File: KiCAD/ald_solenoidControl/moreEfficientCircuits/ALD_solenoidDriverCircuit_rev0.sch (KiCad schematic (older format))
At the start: 36 parts

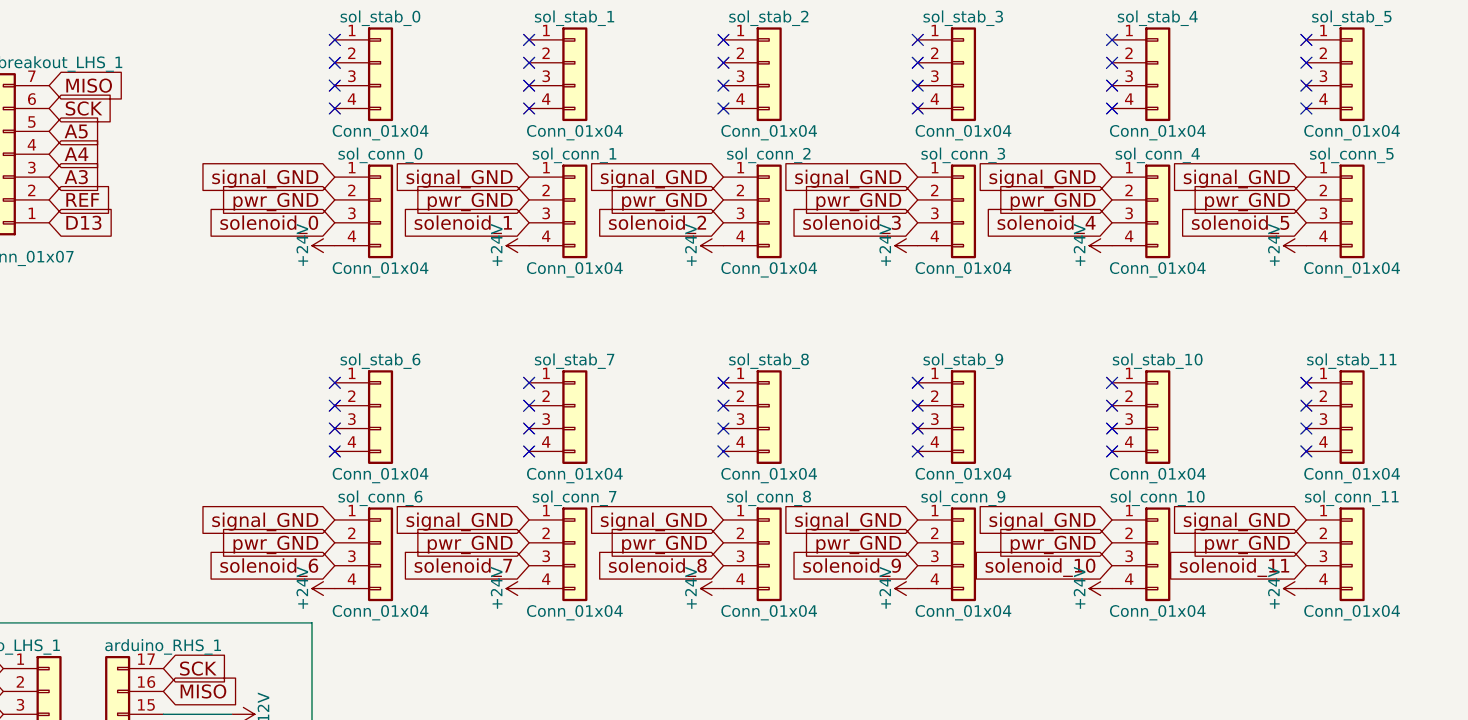
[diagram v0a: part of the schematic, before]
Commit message: add mounting holes to add in card, make zones, move current limiting resistor
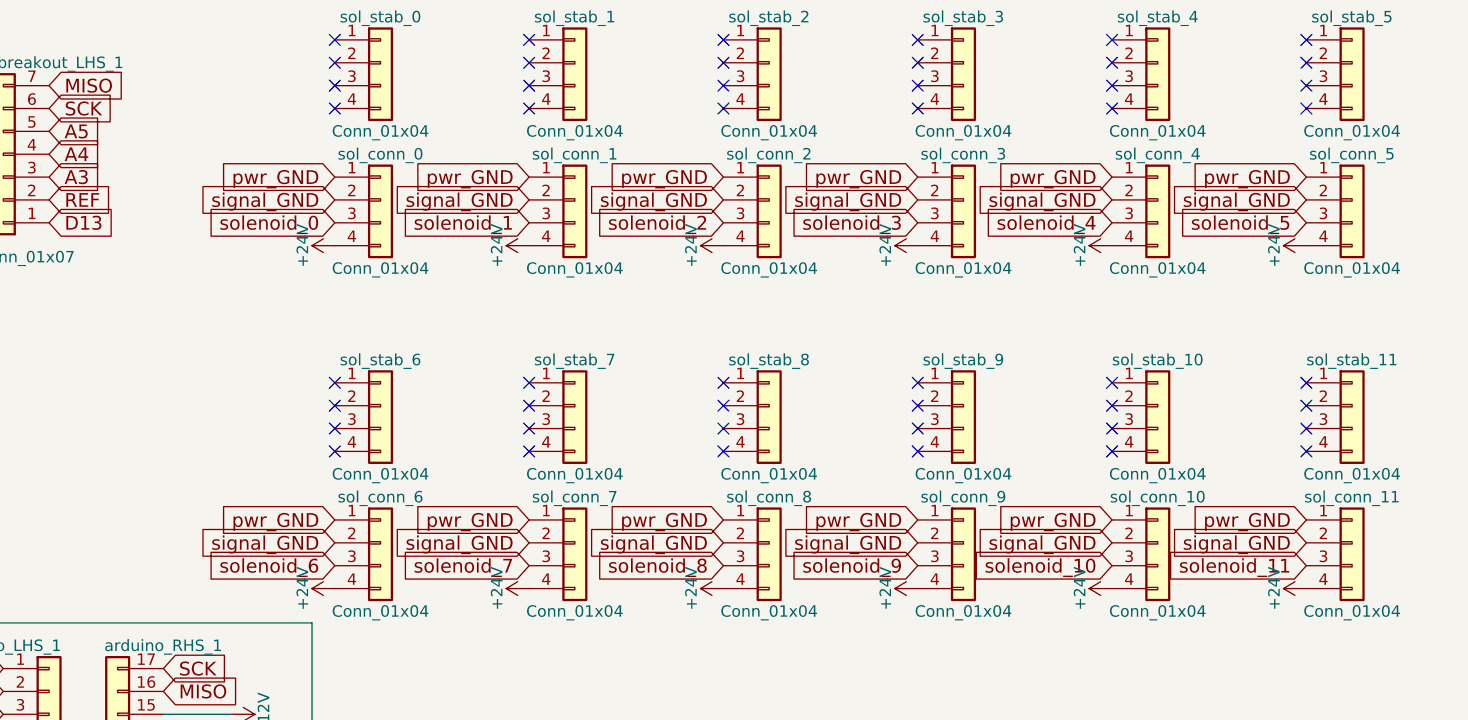
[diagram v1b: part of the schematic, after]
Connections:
- net GNDPWR: now also sol_conn_0.1 (Pin_1), sol_conn_1.1 (Pin_1), sol_conn_10.1 (Pin_1), sol_conn_11.1 (Pin_1), sol_conn_2.1 (Pin_1), sol_conn_3.1 (Pin_1), sol_conn_4.1 (Pin_1), sol_conn_5.1 (Pin_1), sol_conn_6.1 (Pin_1), sol_conn_7.1 (Pin_1), sol_conn_8.1 (Pin_1), sol_conn_9.1 (Pin_1); no longer sol_conn_0.2 (Pin_2), sol_conn_1.2 (Pin_2), sol_conn_10.2 (Pin_2), sol_conn_11.2 (Pin_2), sol_conn_2.2 (Pin_2), sol_conn_3.2 (Pin_2), sol_conn_4.2 (Pin_2), sol_conn_5.2 (Pin_2), sol_conn_6.2 (Pin_2), sol_conn_7.2 (Pin_2), sol_conn_8.2 (Pin_2), sol_conn_9.2 (Pin_2)
- net GNDREF: now also sol_conn_0.2 (Pin_2), sol_conn_1.2 (Pin_2), sol_conn_10.2 (Pin_2), sol_conn_11.2 (Pin_2), sol_conn_2.2 (Pin_2), sol_conn_3.2 (Pin_2), sol_conn_4.2 (Pin_2), sol_conn_5.2 (Pin_2), sol_conn_6.2 (Pin_2), sol_conn_7.2 (Pin_2), sol_conn_8.2 (Pin_2), sol_conn_9.2 (Pin_2); no longer sol_conn_0.1 (Pin_1), sol_conn_1.1 (Pin_1), sol_conn_10.1 (Pin_1), sol_conn_11.1 (Pin_1), sol_conn_2.1 (Pin_1), sol_conn_3.1 (Pin_1), sol_conn_4.1 (Pin_1), sol_conn_5.1 (Pin_1), sol_conn_6.1 (Pin_1), sol_conn_7.1 (Pin_1), sol_conn_8.1 (Pin_1), sol_conn_9.1 (Pin_1)
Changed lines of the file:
@@
 Text GLabel 8200 4650 0    60   Input ~ 0
 solenoid_11
-Text GLabel 3950 4450 0    60   Input ~ 0
-signal_GND
 Text GLabel 5500 5700 0    60   Input ~ 0
 signal_GND
 Text GLabel 5500 6100 0    60   Input ~ 0
-pwr_GND
-Text GLabel 3950 2950 0    60   Input ~ 0
-signal_GND
-Text GLabel 4800 2950 0    60   Input ~ 0
-signal_GND
-Text GLabel 5650 2950 0    60   Input ~ 0
-signal_GND
-Text GLabel 6500 2950 0    60   Input ~ 0
-signal_GND
-Text GLabel 7350 2950 0    60   Input ~ 0
-signal_GND
-Text GLabel 8200 2950 0    60   Input ~ 0
-signal_GND
-Text GLabel 4800 4450 0    60   Input ~ 0
-signal_GND
-Text GLabel 5650 4450 0    60   Input ~ 0
-signal_GND
-Text GLabel 6500 4450 0    60   Input ~ 0
-signal_GND
-Text GLabel 7350 4450 0    60   Input ~ 0
-signal_GND
-Text GLabel 8200 4450 0    60   Input ~ 0
-signal_GND
-Text GLabel 3950 3050 0    60   Input ~ 0
-pwr_GND
-Text GLabel 4800 3050 0    60   Input ~ 0
-pwr_GND
-Text GLabel 5650 3050 0    60   Input ~ 0
-pwr_GND
-Text GLabel 6500 3050 0    60   Input ~ 0
-pwr_GND
-Text GLabel 7350 3050 0    60   Input ~ 0
-pwr_GND
-Text GLabel 8200 3050 0    60   Input ~ 0
-pwr_GND
-Text GLabel 3950 4550 0    60   Input ~ 0
-pwr_GND
-Text GLabel 4800 4550 0    60   Input ~ 0
-pwr_GND
-Text GLabel 5650 4550 0    60   Input ~ 0
-pwr_GND
-Text GLabel 6500 4550 0    60   Input ~ 0
-pwr_GND
-Text GLabel 7350 4550 0    60   Input ~ 0
-pwr_GND
-Text GLabel 8200 4550 0    60   Input ~ 0
 pwr_GND
 $Comp
@@
 Connection ~ 8600 5650
 Connection ~ 3650 5600
+Text GLabel 3950 4550 0    60   Input ~ 0
+signal_GND
+Text GLabel 3950 4450 0    60   Input ~ 0
+pwr_GND
+Text GLabel 4800 4550 0    60   Input ~ 0
+signal_GND
+Text GLabel 4800 4450 0    60   Input ~ 0
+pwr_GND
+Text GLabel 5650 4550 0    60   Input ~ 0
+signal_GND
+Text GLabel 5650 4450 0    60   Input ~ 0
+pwr_GND
+Text GLabel 6500 4550 0    60   Input ~ 0
+signal_GND
+Text GLabel 6500 4450 0    60   Input ~ 0
+pwr_GND
+Text GLabel 7350 4550 0    60   Input ~ 0
+signal_GND
+Text GLabel 7350 4450 0    60   Input ~ 0
+pwr_GND
+Text GLabel 8200 4550 0    60   Input ~ 0
+signal_GND
+Text GLabel 8200 4450 0    60   Input ~ 0
+pwr_GND
+Text GLabel 3950 3050 0    60   Input ~ 0
+signal_GND
+Text GLabel 3950 2950 0    60   Input ~ 0
+pwr_GND
+Text GLabel 4800 3050 0    60   Input ~ 0
+signal_GND
+Text GLabel 4800 2950 0    60   Input ~ 0
+pwr_GND
+Text GLabel 5650 3050 0    60   Input ~ 0
+signal_GND
+Text GLabel 5650 2950 0    60   Input ~ 0
+pwr_GND
+Text GLabel 6500 3050 0    60   Input ~ 0
+signal_GND
+Text GLabel 6500 2950 0    60   Input ~ 0
+pwr_GND
+Text GLabel 7350 3050 0    60   Input ~ 0
+signal_GND
+Text GLabel 7350 2950 0    60   Input ~ 0
+pwr_GND
+Text GLabel 8200 3050 0    60   Input ~ 0
+signal_GND
+Text GLabel 8200 2950 0    60   Input ~ 0
+pwr_GND
 $EndSCHEMATC
